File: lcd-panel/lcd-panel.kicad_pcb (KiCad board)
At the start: 2 copper layers, 85 x 26 mm, 30 parts, among them J1 USB wire, J2 LCD FPC connector, J3 Fan Socket, Q1 AO3400A, U1 FT232HL-REEL, U2 93LC56BT-I/OT, U3 USBLC6-2SC6, Y1 12 MHz, 20 pF load

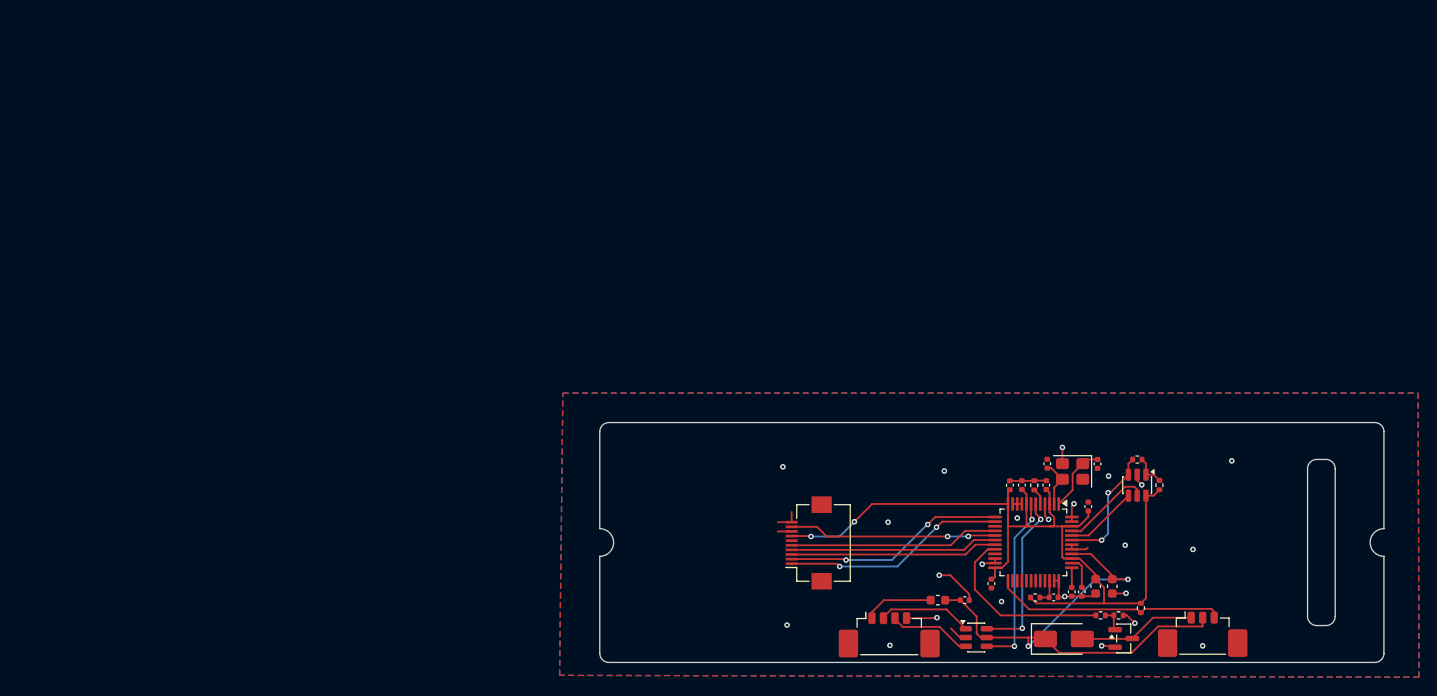
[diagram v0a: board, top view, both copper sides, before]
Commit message: Getting most of the components in roughly in the right places
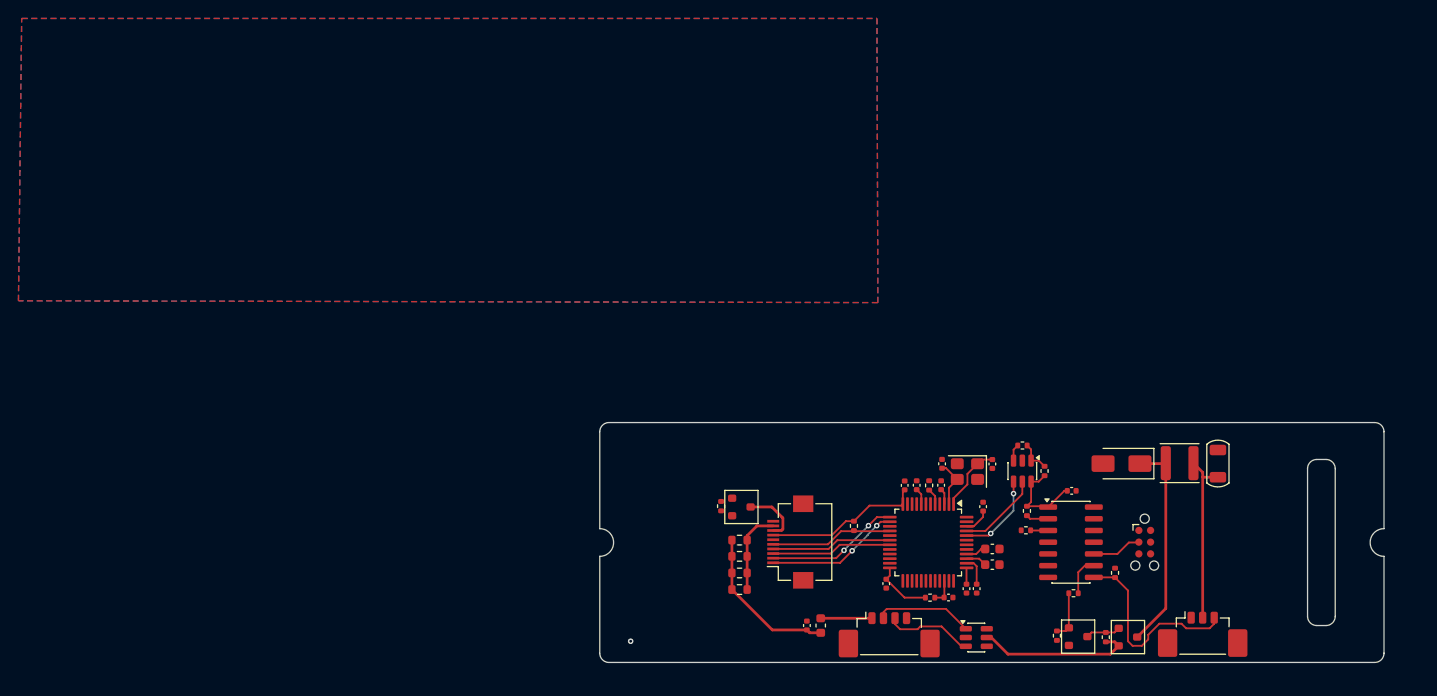
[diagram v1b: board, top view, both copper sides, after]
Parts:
- added C14: 22µF 25V X5R, PCM_Capacitor_SMD_AKL:C_1206_3216Metric, F.Cu at (158.4, 91.5)
- added C15: 100nF (0.1µF), Capacitor_SMD:C_0402_1005Metric, F.Cu at (142.6, 94.4)
- added J4: TC2030, Connector:Tag-Connect_TC2030-IDC-NL_2x03_P1.27mm_Vertical, F.Cu at (150.5, 100.0)
- added L1: 47µH, Inductor_SMD:L_Sunlord_SWPA4018S, F.Cu at (154.3, 91.4)
- added Q2: AO3401A, PCM_Package_TO_SOT_SMD_AKL:SOT-23, F.Cu at (148.7, 110.2)
- added Q3: AO3400A, PCM_Package_TO_SOT_SMD_AKL:SOT-23, F.Cu at (106.8, 96.2)
- added R10: 10kΩ, Resistor_SMD:R_0402_1005Metric, F.Cu at (104.6, 96.1)
- added R11: 10kΩ, Resistor_SMD:R_0402_1005Metric, F.Cu at (119.0, 98.2)
- added R12: 120Ω, Resistor_SMD:R_0603_1608Metric, F.Cu at (106.6, 99.7)
- added R13: 120Ω, Resistor_SMD:R_0603_1608Metric, F.Cu at (106.6, 101.5)
- added R14: 120Ω, Resistor_SMD:R_0603_1608Metric, F.Cu at (106.6, 103.3)
- added R15: 120Ω, Resistor_SMD:R_0603_1608Metric, F.Cu at (106.6, 105.1)
- added R21: 10kΩ, Resistor_SMD:R_0402_1005Metric, F.Cu at (137.8, 96.6)
- added R8: 1kΩ, Resistor_SMD:R_0402_1005Metric, F.Cu at (146.3, 110.3)
- added R9: 100Ω, Resistor_SMD:R_0402_1005Metric, F.Cu at (137.6, 98.7)
- added U4: ATtiny414-SS, Package_SO:SOIC-14_3.9x8.7mm_P1.27mm, F.Cu at (142.5, 100.0)
- Q1: footprint Package_TO_SOT_SMD:SOT-23 -> PCM_Package_TO_SOT_SMD_AKL:SOT-23
- moved D1 20.0 mm to (148.0, 91.5), turned to 180 degrees
- moved C9 17.3 mm to (113.9, 109.0), turned to 90 degrees
- moved C1 13.6 mm to (134.0, 100.7), turned to 0 degrees
- moved FB1 13.0 mm to (115.4, 109.0), turned to -90 degrees
- moved R6 12.5 mm to (137.3, 89.5)
- moved R7 12.5 mm to (139.7, 92.3)
- moved U2 12.5 mm to (137.2, 92.3)
- moved C8 11.4 mm to (134.0, 102.4), turned to 0 degrees
- moved C12 11.4 mm to (131.2, 105.0)
- moved C11 11.4 mm to (132.3, 105.0)
- moved C10 11.4 mm to (128.4, 93.8)
- moved C13 11.4 mm to (129.2, 106.0)
- moved C3 11.4 mm to (134.0, 91.5)
- moved C4 11.4 mm to (124.5, 93.8)
- moved C5 11.4 mm to (122.5, 104.5)
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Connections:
- net LCD_MOSI renamed MOSI
- net LCD_SCK renamed SCK
- D1 pad 1: +5V -> Net-(D1-K)
- D1 pad 2: Net-(D1-A) -> GND
- J2 pad 8: GND -> Net-(J2-Pin_8)
- J2 pad 9: LCD_BL -> Net-(J2-Pin_9)
- J3 pad 1: Net-(D1-A) -> GND
- J3 pad 2: +5V -> /Fan VDD
- J3 pad 3: FAN TACH -> TACH
- Q1 pad 3: Net-(D1-A) -> Net-(Q1-D)
- R2 pad 1: FAN GATE -> Net-(Q1-G)
- R2 pad 2: Net-(Q1-G) -> FAN
- R5 pad 1: FAN TACH -> TACH
- U1 pad 15: unconnected-(U1-ADBUS2-Pad15) -> MISO
- U1 pad 17: LCD_BL -> SEL/DTR#
- U1 pad 20: FAN GATE -> unconnected-(U1-ADBUS7-Pad20)
- U1 pad 21: unconnected-(U1-ACBUS0-Pad21) -> /SS TINY
- U1 pad 25: FAN TACH -> unconnected-(U1-ACBUS1-Pad25)
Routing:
- net +3V3: track 94.2 -> 41.9 mm, vias 2 -> 0
- net GND: track 41.6 -> 0.00 mm, vias 23 -> 1
- net FAN TACH: track 25.2 -> 0.00 mm
- net Net-(D1-K): track 0.00 -> 23.0 mm
- net TACH: track 0.00 -> 21.7 mm
- net +5V: track 56.8 -> 36.2 mm, vias 2 -> 0
- net LCD_BL: track 22.5 -> 1.91 mm, vias 2 -> 0
- net FAN GATE: track 20.0 -> 0.00 mm
- net D+: track 19.3 -> 0.00 mm, vias 2 -> 0
- net /Fan VDD: track 0.00 -> 18.8 mm
- net D-: track 18.4 -> 0.00 mm, vias 2 -> 0
- net Net-(D1-A): track 12.8 -> 0.00 mm
- net EEDATA: track 13.5 -> 1.82 mm, vias 2 -> 0
- net MOSI: track 24.2 -> 14.5 mm
- net SCK: track 24.0 -> 14.5 mm
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
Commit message: Wiring most of the components together
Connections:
- U1 pad 17: SEL/DTR# -> unconnected-(U1-ADBUS4-Pad17)
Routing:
- net +3V3: track 41.9 -> 83.5 mm, vias 0 -> 2
- net Net-(Q3-G): track 0.00 -> 38.3 mm, vias 0 -> 2
- net +5V: track 36.2 -> 68.4 mm, vias 0 -> 3
- net MISO: track 0.00 -> 23.5 mm, vias 0 -> 2
- net MOSI: track 14.5 -> 37.6 mm, vias 2 -> 4
- net SCK: track 14.5 -> 36.8 mm, vias 2 -> 4
- net D+: track 0.00 -> 19.7 mm, vias 0 -> 2
- net /SS TINY: track 2.44 -> 19.1 mm, vias 0 -> 2
- net D-: track 0.00 -> 16.0 mm, vias 0 -> 2
- net EEDATA: track 1.82 -> 13.9 mm, vias 0 -> 2
- net GND: track 0.00 -> 8.79 mm, vias 1 -> 2
- net EECS: track 9.04 -> 11.7 mm
- net EECLK: track 9.36 -> 9.66 mm, vias 2 -> 0
